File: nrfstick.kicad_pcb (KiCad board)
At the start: 4 copper layers, 13.6 x 17.4 mm, 28 parts, among them J1 USB_A, J2 programming conn, SW4 SW_Push, U3 APX803L20-27SR-7, U4 CP2102C-Axx-xQFN24, U5 BM15C, Y1 32.768kHz

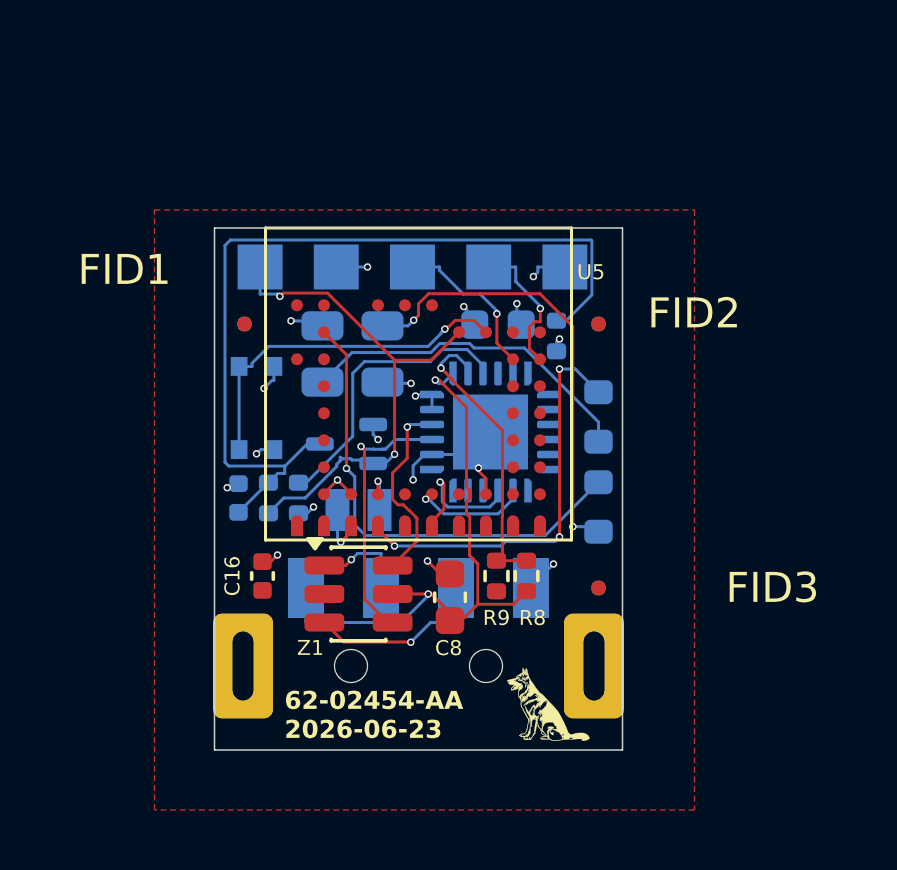
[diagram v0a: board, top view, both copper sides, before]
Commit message: Replace SW4 with Alps SKRPABE010 and save revised PCB layout
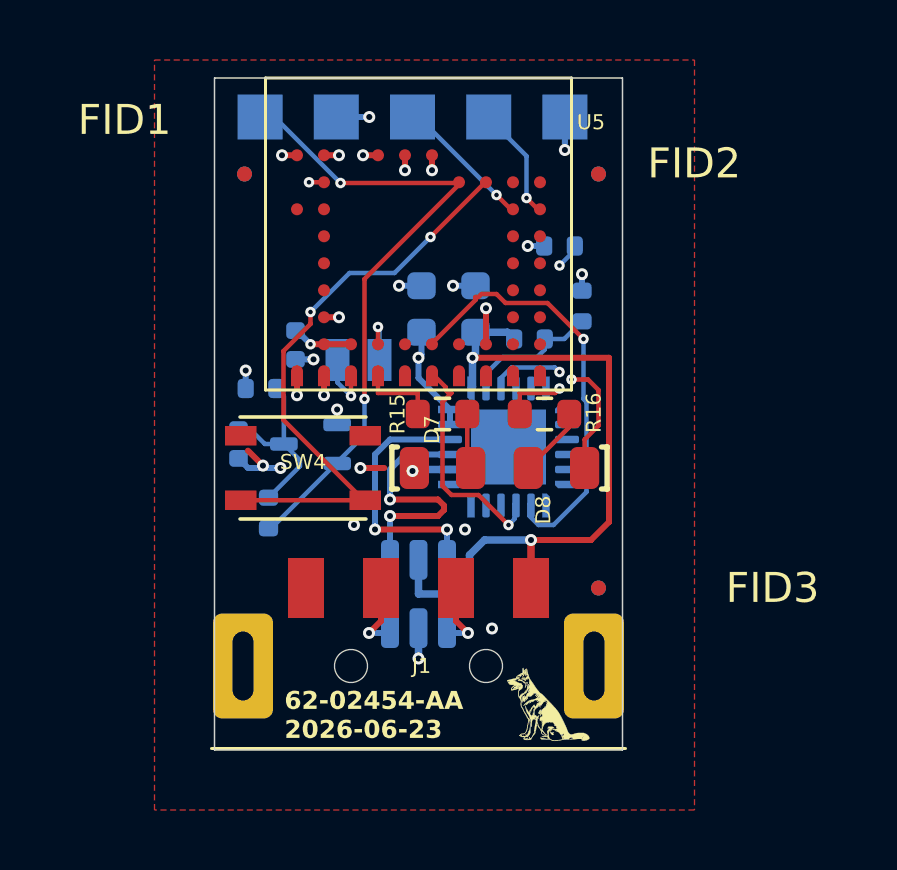
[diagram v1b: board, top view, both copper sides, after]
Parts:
- C16, C8, R8, R9, Z1: moved to B.Cu
- D7, D8, J1, R15, R16: moved to F.Cu
- SW4: value SW_Push -> SKRPABE010; footprint footprint:SW_STU-057A23AC_8127_2.25N -> footprint:SW_Push_Alps_SKRPABE010; moved to F.Cu
- moved R7 12.1 mm to (111.5, 83.2), turned to 0 degrees
- moved R29 10.0 mm to (101.5, 88.0), turned to 0 degrees
- moved C8 9.65 mm to (108.7, 85.3)
- moved R9 9.44 mm to (112.2, 85.2), turned to 90 degrees
- moved R8 7.90 mm to (110.5, 86.3), turned to 0 degrees
- moved C16 7.78 mm to (102.7, 86.5)
- moved D8 6.93 mm to (111.4, 90.6), turned to 180 degrees
- moved D7 5.52 mm to (107.6, 90.6), turned to 0 degrees
- moved R15 5.20 mm to (107.6, 88.8), turned to 0 degrees
- moved FID1 5.00 mm to (101.0, 80.8)
- moved FID2 5.00 mm to (112.8, 80.8)
- moved FID4 5.00 mm to (101.0, 80.8)
- moved FID5 5.00 mm to (112.8, 80.8)
- moved J2 5.00 mm to (106.6, 78.9)
- moved U5 5.00 mm to (106.8, 80.0)
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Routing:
- net Net-(U3-VCC): track 28.7 -> 6.11 mm
- net Net-(D8-A): track 15.1 -> 2.36 mm, vias 2 -> 0
- net /LED_BLUE: track 13.9 -> 2.75 mm, vias 3 -> 0
- net /UART_nRF_TX: track 3.88 -> 14.6 mm
- net Net-(D7-A): track 11.5 -> 1.85 mm
- net /BUTTON: track 11.9 -> 19.6 mm, vias 1 -> 2
- net GND: track 13.3 -> 20.1 mm, vias 12 -> 24
- net Net-(U4-VBUS): track 9.89 -> 4.63 mm, vias 1 -> 0
- net /~{RESET}: track 17.4 -> 22.1 mm
- net +5V: track 19.8 -> 24.2 mm
- net Net-(J1-D+): track 6.08 -> 2.43 mm
- net /UART_nRF_RX: track 4.57 -> 7.93 mm
- net Net-(U4-~{RST}): track 9.71 -> 6.92 mm, vias 0 -> 2
- net Net-(U4-D-): track 6.46 -> 8.62 mm, vias 1 -> 2
- net /LED_RED: track 15.9 -> 13.8 mm, vias 1 -> 2
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- added copper zone on In2.Cu, net GND
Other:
- board size 13.6 x 17.4 mm -> 13.6 x 22.4 mm

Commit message: panel layout using kikit, not routed
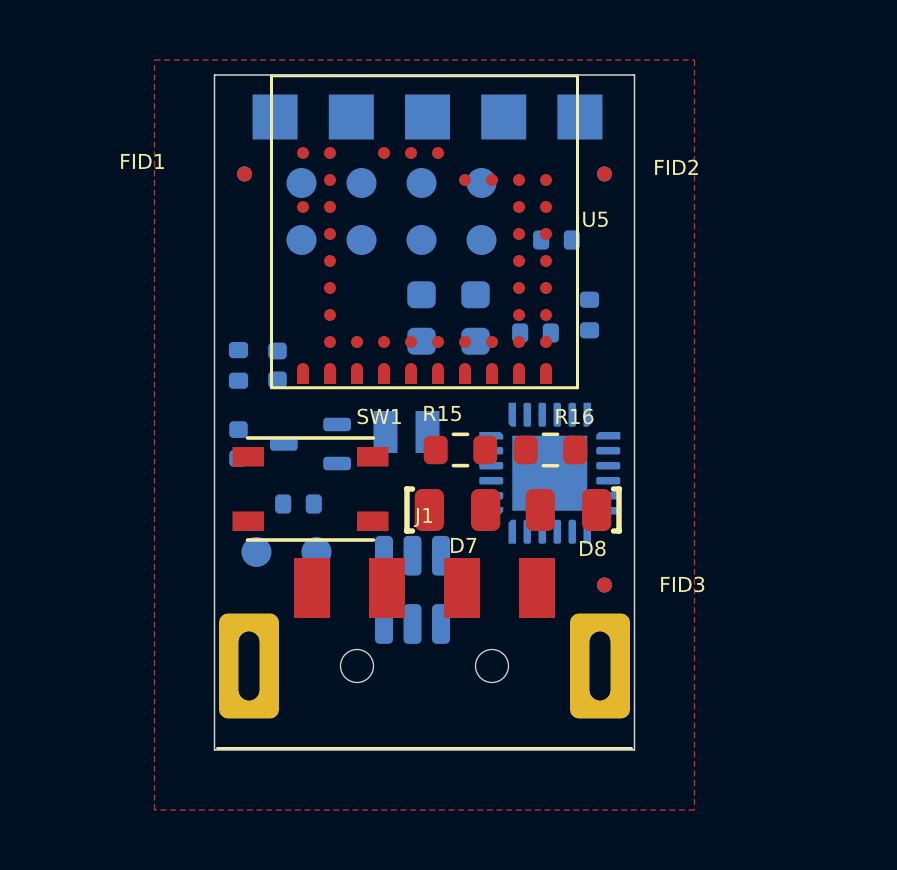
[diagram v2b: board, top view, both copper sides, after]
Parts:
- added J3: IO00, footprint:Conn_Pads_1x04_P2.00mm_D1.00mm, B.Cu at (105.9, 81.1)
- added J4: Reset, footprint:Conn_Pads_2x01_P2.00mm_D1.00mm, B.Cu at (102.4, 93.4)
- added J6: UART2, footprint:Conn_Pads_1x04_P2.00mm_D1.00mm, B.Cu at (105.9, 83.0)
- H2: moved to B.Cu
- R29: value 1.00K -> 1.00k
- moved H2 3.75 mm to (110.4, 94.8), turned to 180 degrees
- moved Y1 2.88 mm to (106.4, 89.4)
- moved U4 1.63 mm to (111.2, 90.8)
- moved D7 1.49 mm to (108.1, 92.0)
- moved D8 1.46 mm to (111.8, 92.0)
- moved R15 1.34 mm to (108.2, 90.0)
- moved R16 1.22 mm to (111.2, 90.0)
- moved R29 1.07 mm to (100.8, 87.2), turned to -90 degrees
- moved R17 1.04 mm to (102.8, 91.8), turned to 180 degrees
- moved C16 0.91 mm to (102.1, 87.2)
- moved SW1 0.74 mm to (103.2, 91.3), turned to 180 degrees
- moved J2 0.50 mm to (107.1, 78.9)
- moved R9 0.39 mm to (112.5, 85.5)
- moved C7 0.30 mm to (106.9, 85.6)
- moved C8 0.30 mm to (108.7, 85.6)
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- renumbered SW4 to SW1
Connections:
- U4 pad 18: unconnected-(U4-~{CTS}-Pad18) -> /UART_nRF_RTS
- U4 pad 19: unconnected-(U4-~{RTS}-Pad19) -> /UART_nRF_CTS
- U5 pad G8: unconnected-(U5-P1.08-PadG8) -> /UART_nRF_RTS
- U5 pad G9: unconnected-(U5-P1.07/AIN3-PadG9) -> /UART_nRF_CTS
- U5 pad H9: unconnected-(U5-P2.00-PadH9) -> Net-(J6-Pin_4)
- U5 pad J2: unconnected-(U5-P0.03-PadJ2) -> Net-(J3-Pin_1)
- U5 pad J4: unconnected-(U5-P0.00-PadJ4) -> Net-(J3-Pin_4)
- U5 pad J7: unconnected-(U5-P2.03-PadJ7) -> Net-(J6-Pin_1)
- U5 pad J8: unconnected-(U5-P2.02-PadJ8) -> Net-(J6-Pin_2)
- U5 pad J9: unconnected-(U5-P2.01-PadJ9) -> Net-(J6-Pin_3)
- U5 pad K2: unconnected-(U5-P0.02-PadK2) -> Net-(J3-Pin_2)
- U5 pad K4: unconnected-(U5-P0.01-PadK4) -> Net-(J3-Pin_3)
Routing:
- net +5V: track 24.2 -> 0.00 mm, vias 2 -> 0
- net /~{RESET}: track 22.1 -> 0.00 mm, vias 2 -> 0
- net GND: track 20.1 -> 0.00 mm, vias 24 -> 0
- net /BUTTON: track 19.6 -> 0.00 mm, vias 2 -> 0
- net /UART_nRF_TX: track 14.6 -> 0.00 mm, vias 1 -> 0
- net /LED_RED: track 13.8 -> 0.00 mm, vias 2 -> 0
- net Net-(U4-D-): track 8.62 -> 0.00 mm, vias 2 -> 0
- net Net-(U4-D+): track 8.59 -> 0.00 mm, vias 2 -> 0
- net /UART_nRF_RX: track 7.93 -> 0.00 mm, vias 1 -> 0
- net VDD: track 7.84 -> 0.00 mm, vias 5 -> 0
- net Net-(U4-~{RST}): track 6.92 -> 0.00 mm, vias 2 -> 0
- net Net-(J4-Pin_2): track 6.11 -> 0.00 mm
- net Net-(J2-Pin_3): track 4.64 -> 0.00 mm, vias 1 -> 0
- net Net-(U4-VBUS): track 4.63 -> 0.00 mm
- net Net-(J2-Pin_2): track 3.90 -> 0.00 mm, vias 1 -> 0
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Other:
- board size 13.6 x 22.4 mm -> 14 x 22.5 mm
- board text added: "62-02454-AB 2026-09-10"
- board text added: "P0: 0 1 2 3"
- board text added: "P2: 0 1 2 3"
- board text removed: "62-02454-AA 2026-06-23"

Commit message: panelize, new usb connector
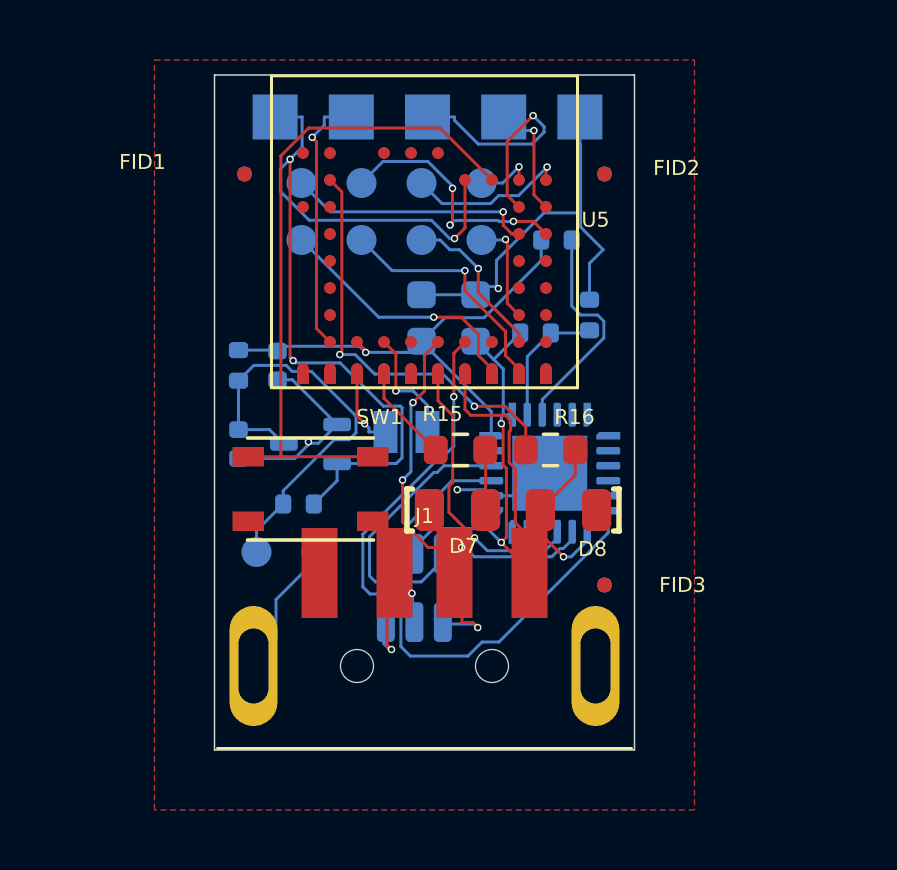
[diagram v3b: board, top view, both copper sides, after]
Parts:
- J1: footprint footprint:connector-USB-A-male-smd-Molex-480372100 -> footprint:USB_A_AdamTech_USB-AP-S-RA-SMT
- moved Z1 0.09 mm to (106.7, 94.6)
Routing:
- net GND: track 0.00 -> 29.3 mm, vias 0 -> 4
- net /~{RESET}: track 0.00 -> 28.8 mm, vias 0 -> 3
- net VDD: track 0.00 -> 26.6 mm, vias 0 -> 2
- net /BUTTON: track 0.00 -> 22.3 mm
- net /UART_nRF_RTS: track 0.00 -> 22.2 mm, vias 0 -> 1
- net +5V: track 0.00 -> 14.9 mm, vias 0 -> 2
- net Net-(J4-Pin_2): track 0.00 -> 14.4 mm
- net /LED_RED: track 0.00 -> 14.0 mm, vias 0 -> 2
- net /UART_nRF_TX: track 0.00 -> 13.1 mm, vias 0 -> 3
- net /UART_nRF_CTS: track 0.00 -> 9.92 mm, vias 0 -> 1
- net /UART_nRF_RX: track 0.00 -> 9.56 mm, vias 0 -> 1
- net Net-(U4-D-): track 0.00 -> 9.30 mm
- net Net-(J2-Pin_3): track 0.00 -> 8.76 mm, vias 0 -> 1
- net Net-(J6-Pin_4): track 0.00 -> 8.54 mm, vias 0 -> 1
- net Net-(J3-Pin_3): track 0.00 -> 8.50 mm, vias 0 -> 3
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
